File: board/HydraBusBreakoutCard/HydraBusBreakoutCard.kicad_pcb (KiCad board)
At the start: 2 copper layers, 106.7 x 105.4 mm, 15 parts, among them J1 Bus_Hydra_8bit, J10 I2C, J11 Power, J2 Data Bus, J3 Address Bus, J4 SPI, J5 Interrupts & I/O, J6 Clocks, J7 Bus Control, J8 Reset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

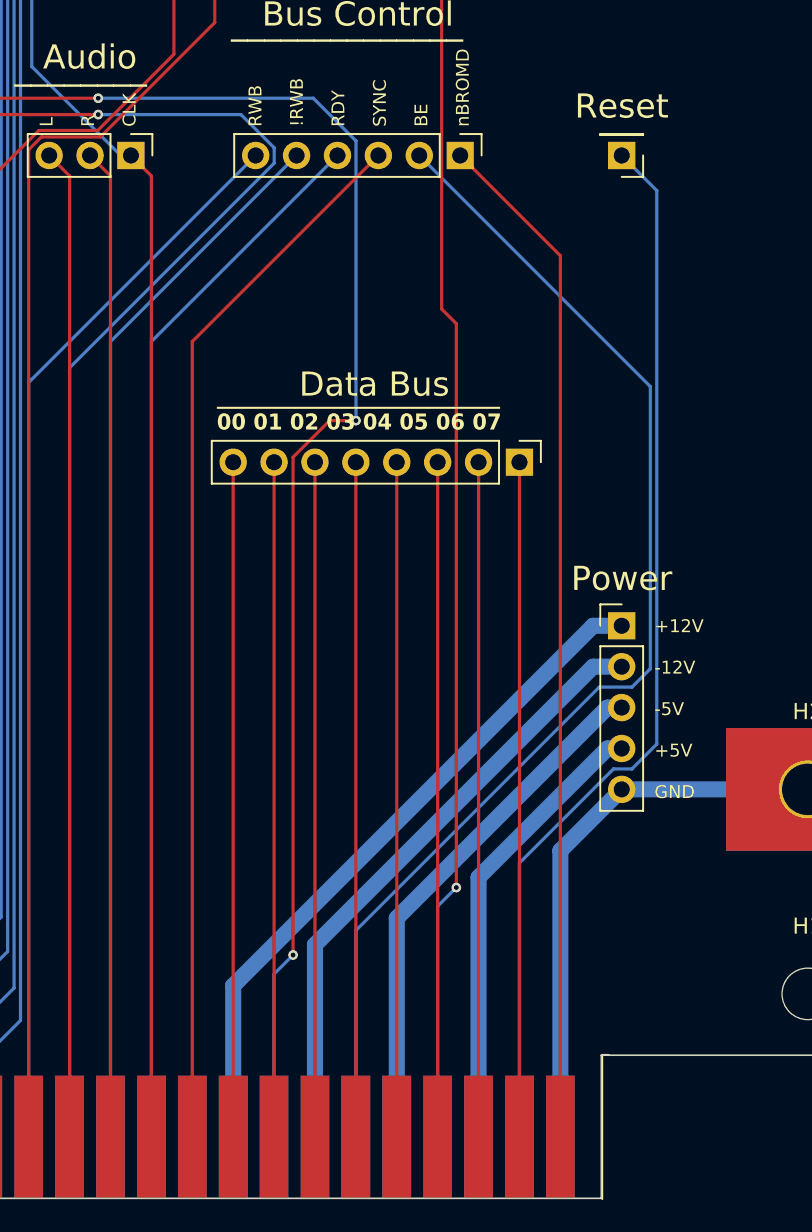
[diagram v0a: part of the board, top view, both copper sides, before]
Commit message: Board version 0.6F, moving stuff around and updating the silkscreen to be more consistent.
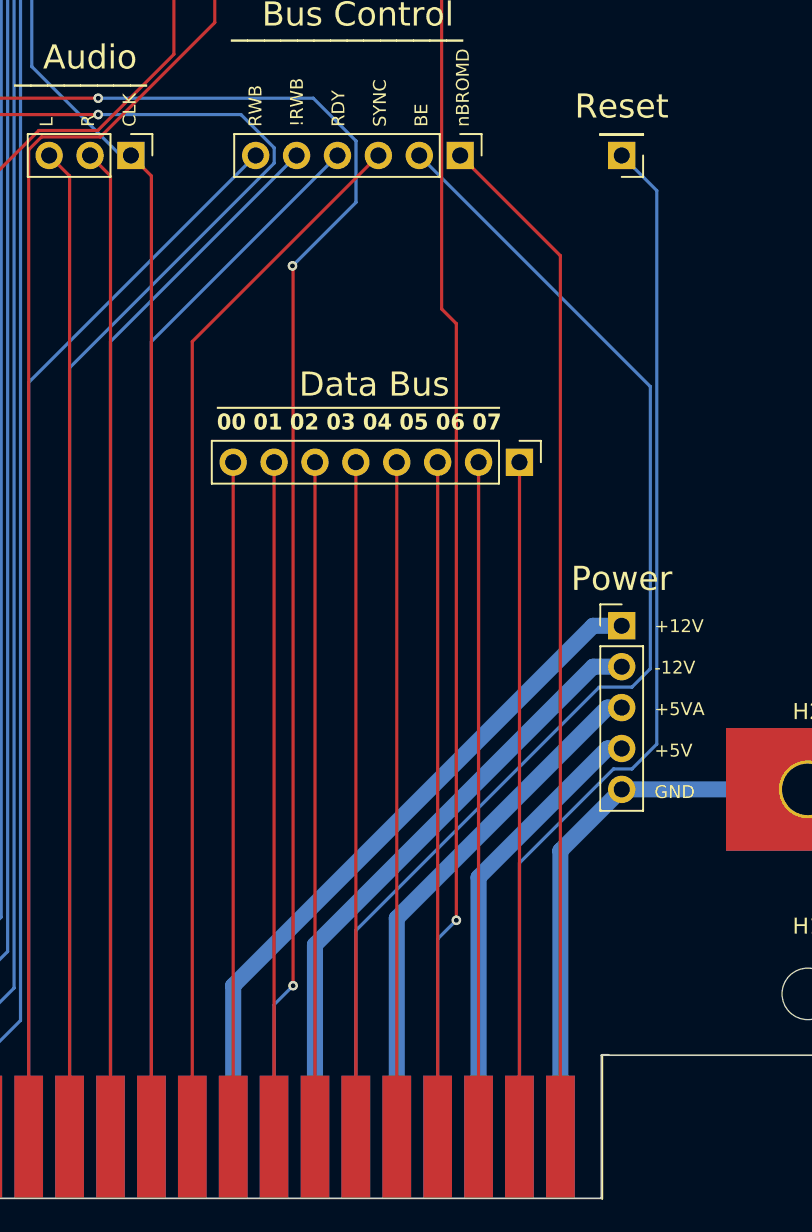
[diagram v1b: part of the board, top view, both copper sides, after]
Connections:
- net -5V renamed +5VA
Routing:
- net SER_CLK: track 94.7 -> 93.8 mm
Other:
- board text added: "+12V -12V +5VA +5V GND"
- board text removed: "+12V -12V -5V +5V GND"

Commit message: Board V1.1G
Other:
- board text added: "SYNC !RWB RWB RDY BE nBROMD"
- board text removed: "RWB !RWB RDY SYNC BE nBROMD"

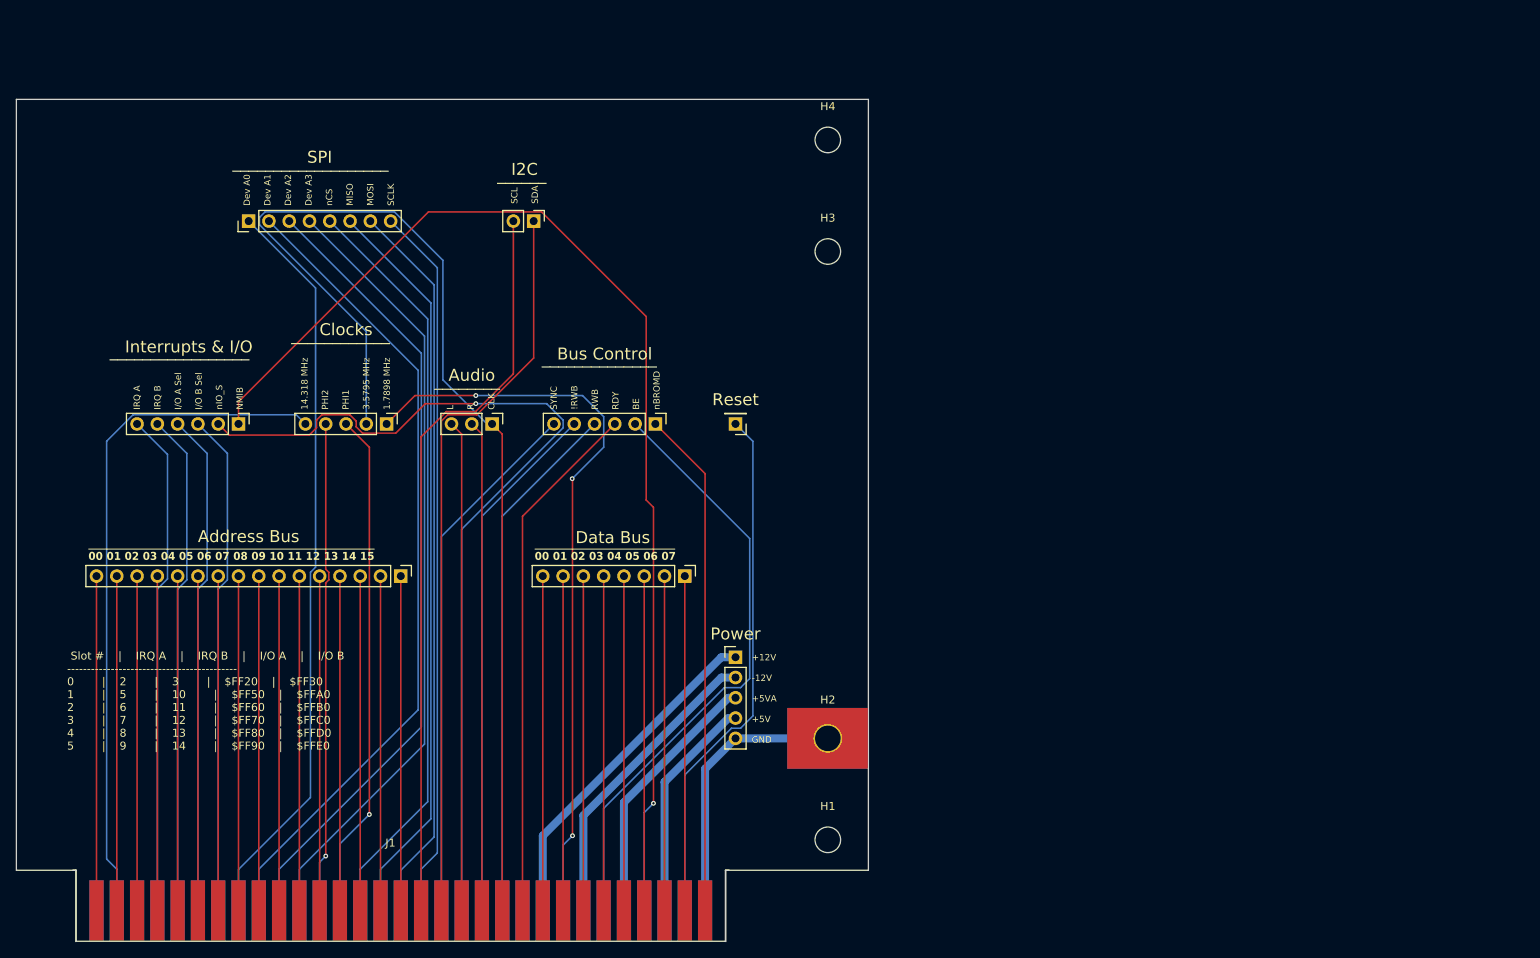
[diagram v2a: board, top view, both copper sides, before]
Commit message: V2.0 updates and new hydra breakout and counter cards.
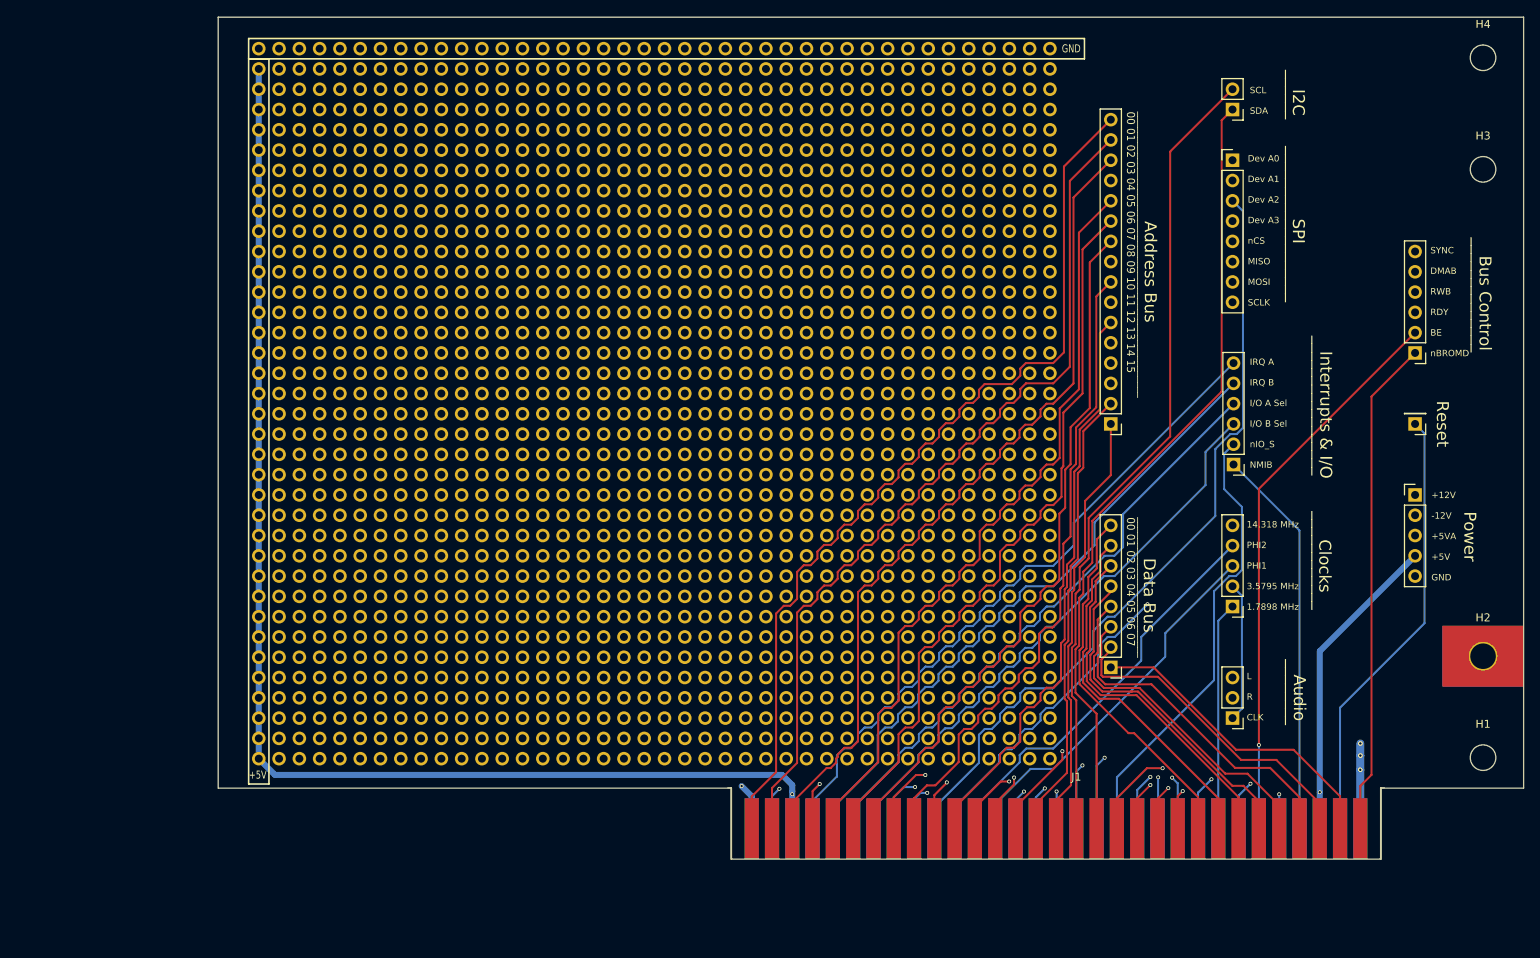
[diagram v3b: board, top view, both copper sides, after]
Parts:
- added J17: Conn_02x40_Odd_Even, CustomLibrary:Holes_2x40_P2.54mm, F.Cu at (193.0, 41.9)
- added J18: Conn_02x40_Odd_Even, CustomLibrary:Holes_2x40_P2.54mm, F.Cu at (193.0, 47.0)
- added J19: Conn_02x40_Odd_Even, CustomLibrary:Holes_2x40_P2.54mm, F.Cu at (193.0, 52.1)
- added J20: Conn_02x40_Odd_Even, CustomLibrary:Holes_2x40_P2.54mm, F.Cu at (193.0, 57.1)
- added J21: Conn_02x40_Odd_Even, CustomLibrary:Holes_2x40_P2.54mm, F.Cu at (193.0, 62.2)
- added J22: Conn_02x40_Odd_Even, CustomLibrary:Holes_2x40_P2.54mm, F.Cu at (193.0, 67.3)
- added J23: Conn_02x40_Odd_Even, CustomLibrary:Holes_2x40_P2.54mm, F.Cu at (193.0, 72.4)
- added J24: Conn_02x40_Odd_Even, CustomLibrary:Holes_2x40_P2.54mm, F.Cu at (193.0, 77.5)
- added J25: Conn_02x40_Odd_Even, CustomLibrary:Holes_2x40_P2.54mm, F.Cu at (193.0, 82.5)
- added J26: Conn_02x40_Odd_Even, CustomLibrary:Holes_2x40_P2.54mm, F.Cu at (193.0, 87.6)
- added J27: Conn_02x40_Odd_Even, CustomLibrary:Holes_2x40_P2.54mm, F.Cu at (193.0, 92.7)
- added J28: Conn_02x40_Odd_Even, CustomLibrary:Holes_2x40_P2.54mm, F.Cu at (193.0, 97.8)
- added J29: Conn_02x40_Odd_Even, CustomLibrary:Holes_2x40_P2.54mm, F.Cu at (193.0, 102.9)
- added J30: Conn_02x40_Odd_Even, CustomLibrary:Holes_2x40_P2.54mm, F.Cu at (193.0, 108.0)
- added J31: Conn_02x40_Odd_Even, CustomLibrary:Holes_2x40_P2.54mm, F.Cu at (193.0, 113.0)
- added J32: Conn_02x40_Odd_Even, CustomLibrary:Holes_2x40_P2.54mm, F.Cu at (193.0, 118.1)
- added J33: Conn_02x40_Odd_Even, CustomLibrary:Holes_2x40_P2.54mm, F.Cu at (193.0, 123.2)
- added J34: Conn_02x40_Odd_Even, CustomLibrary:Holes_2x40_P2.54mm, F.Cu at (193.0, 128.3)
- moved J5 124.7 mm to (216.0, 94.0), turned to 180 degrees
- moved J4 123.4 mm to (215.9, 55.9), turned to 0 degrees
- moved J6 108.4 mm to (215.9, 111.8), turned to 180 degrees
- moved J9 99.8 mm to (215.9, 125.7), turned to 180 degrees
- moved J7 95.5 mm to (238.8, 80.0), turned to 180 degrees
- moved J3 90.9 mm to (200.7, 88.9), turned to 180 degrees
- moved J10 88.6 mm to (215.9, 49.5), turned to 180 degrees
- moved J11 87.5 mm to (238.8, 97.8)
- moved J8 85.1 mm to (238.8, 88.9)
- moved J1 82.7 mm to (192.5, 140.1)
- moved H1 82.7 mm to (247.3, 130.7)
- moved H2 82.7 mm to (247.3, 118.0)
- moved H3 82.7 mm to (247.3, 57.0)
- moved H4 82.7 mm to (247.3, 43.1)
- moved J2 54.6 mm to (200.7, 119.4), turned to 180 degrees
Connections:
- net !RWB renamed DMAB
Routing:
- net +5V: track 28.3 -> 266.4 mm, vias 0 -> 2
- net AUDIO_CLK: track 142.1 -> 35.2 mm, vias 0 -> 1
- net NMIB: track 144.4 -> 49.0 mm, vias 1 -> 0
- net Net-(J1-A00): track 41.9 -> 116.4 mm
- net Net-(J1-A01): track 41.9 -> 111.4 mm
- net SER_CLK: track 93.8 -> 28.5 mm, vias 3 -> 0
- net Net-(J1-A02): track 41.9 -> 106.1 mm
- net Net-(J1-A03): track 41.9 -> 102.3 mm, vias 0 -> 1
- net nIO_S: track 115.8 -> 56.5 mm, vias 1 -> 0
- net Net-(J1-A04): track 41.9 -> 97.6 mm
- net Net-(J1-A05): track 41.9 -> 93.5 mm
- net Net-(J1-A06): track 41.9 -> 89.4 mm
- net Net-(J1-A07): track 41.9 -> 86.1 mm, vias 0 -> 1
- net Net-(J1-A08): track 41.9 -> 81.8 mm
- net Net-(J1-SND_CR): track 61.5 -> 21.8 mm, vias 0 -> 1
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- added copper zone on In2.Cu, net GND
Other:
- board size 106.7 x 105.4 mm -> 163.4 x 105.4 mm
- copper layers 2 -> 4
- board text added: "+5V"
- board text added: "GND"
- board text added: "SYNC DMAB RWB RDY BE nBROMD"
- board text removed: "SYNC !RWB RWB RDY BE nBROMD"
- board text removed: "Slot # | IRQ A | IRQ B | I/O A | I/O B ------------------------------------------- 0 | 2 | 3 | $FF20 | $FF30 1 | 5 | 10 | $FF50 | $FFA0 2 | 6 | 11 | $FF60 | $FFB0 3 | 7 | 12 | $FF70 | $FFC0 4 | 8 | 13 | $FF80 | $FFD0 5 | 9 | 14 | $FF90 | $FFE0"
